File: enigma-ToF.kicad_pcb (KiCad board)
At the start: 2 copper layers, 90 x 90 mm, 16 parts, among them J1 Conn_01x05, U0 PCF8575, U1 VL53L1X, U10 VL53L1X, U15 PCF8575, U2 VL53L1X, U3 VL53L1X, U4 VL53L1X, U5 VL53L1X, U6 VL53L1X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

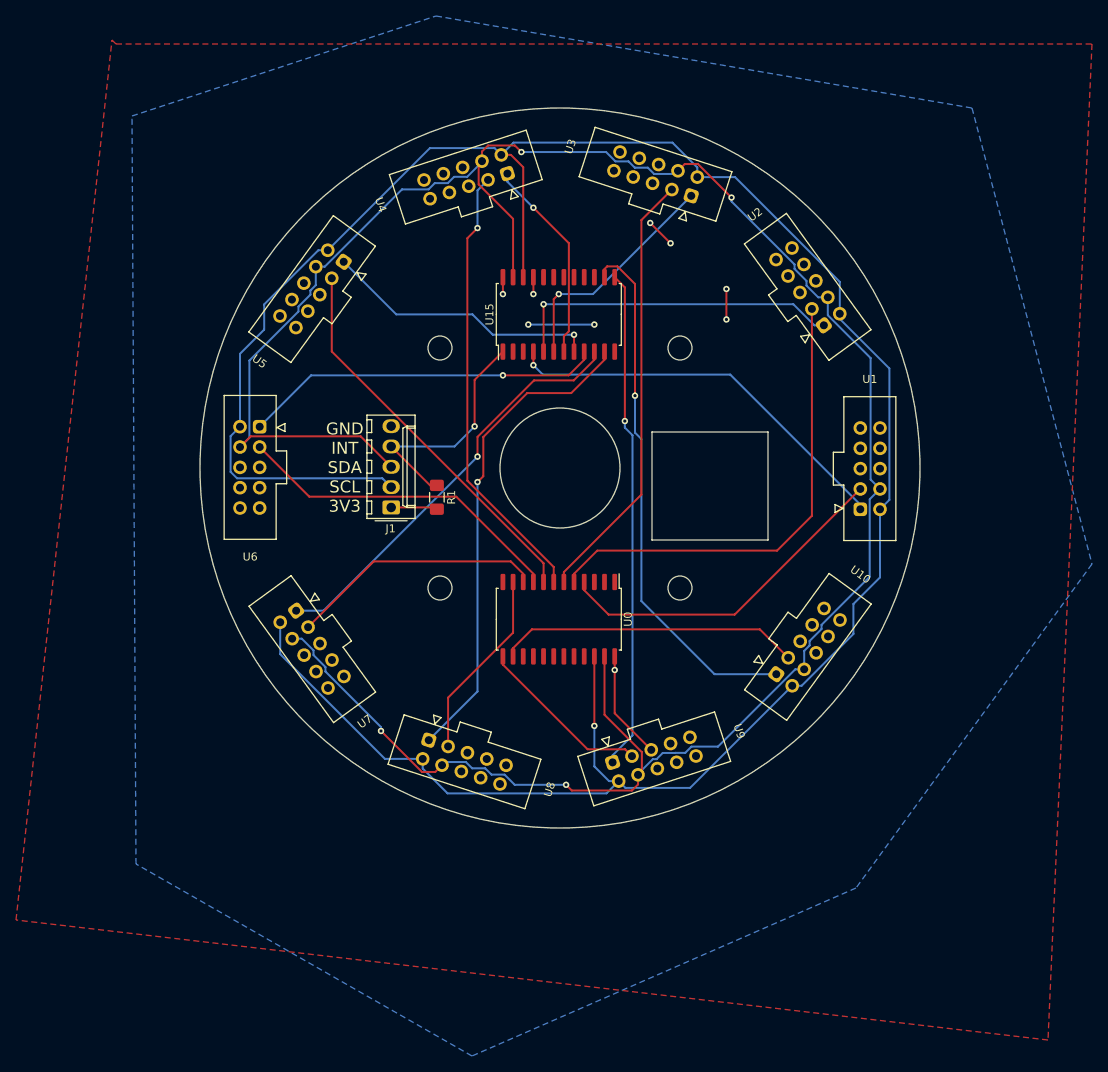
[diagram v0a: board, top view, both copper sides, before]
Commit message: Add touchpoints and power LED
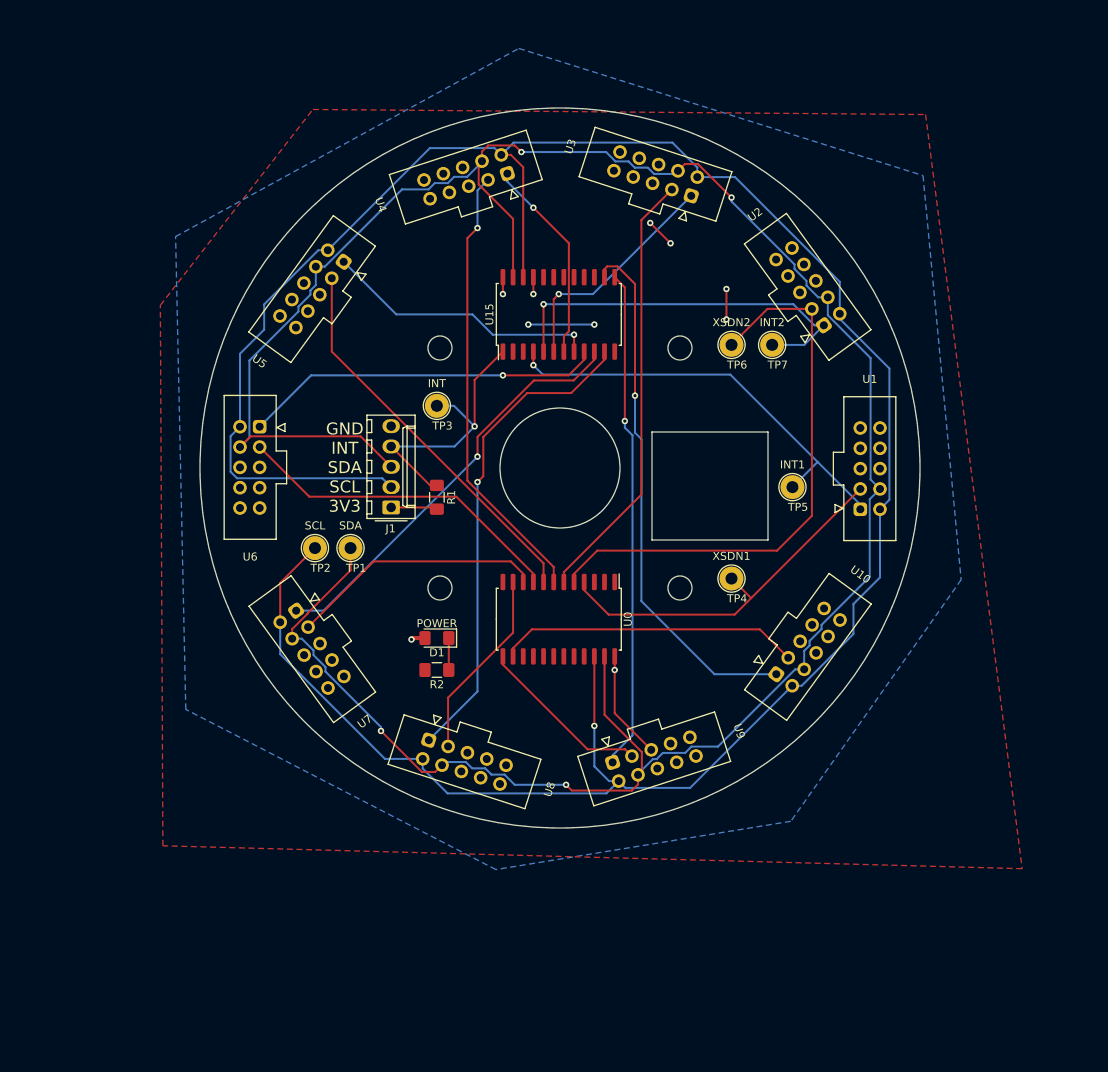
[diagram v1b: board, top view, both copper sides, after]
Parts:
- added D1: POWER, LED_SMD:LED_1206_3216Metric_Pad1.42x1.75mm_HandSolder, F.Cu at (54.6, 91.3)
- added R2: R, Resistor_SMD:R_1206_3216Metric_Pad1.42x1.75mm_HandSolder, F.Cu at (54.6, 95.2)
- added TP1: SDA, TestPoint:TestPoint_Loop_D2.54mm_Drill1.5mm_Beaded, F.Cu at (43.8, 80.0)
- added TP2: SCL, TestPoint:TestPoint_Loop_D2.54mm_Drill1.5mm_Beaded, F.Cu at (39.4, 80.0)
- added TP3: INT, TestPoint:TestPoint_Loop_D2.54mm_Drill1.5mm_Beaded, F.Cu at (54.6, 62.2)
- added TP4: XSDN1, TestPoint:TestPoint_Loop_D2.54mm_Drill1.5mm_Beaded, F.Cu at (91.4, 83.8)
- added TP5: INT1, TestPoint:TestPoint_Loop_D2.54mm_Drill1.5mm_Beaded, F.Cu at (99.1, 72.4)
- added TP6: XSDN2, TestPoint:TestPoint_Loop_D2.54mm_Drill1.5mm_Beaded, F.Cu at (91.4, 54.6)
- added TP7: INT2, TestPoint:TestPoint_Loop_D2.54mm_Drill1.5mm_Beaded, F.Cu at (96.5, 54.6)
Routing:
- net /SDA: track 295.8 -> 310.1 mm
- net /XSDN2: track 59.6 -> 71.5 mm
- net /SCL: track 308.1 -> 319.2 mm
- net /INT2: track 42.0 -> 49.5 mm
- net /INT: track 30.0 -> 35.8 mm
- net /INT1: track 50.4 -> 54.8 mm
- net Net-(D1-Pad1): track 0.00 -> 3.99 mm
- net /XSDN1: track 43.3 -> 46.8 mm
- net +3V3: track 31.0 -> 32.8 mm, vias 7 -> 8
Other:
- board text added: "The PCB is a circle of 90mm in diameter It has a 15mm diameter hole in its center and another squarish hole. It has 4 mounting points of 3mm diameter for M3 screws."

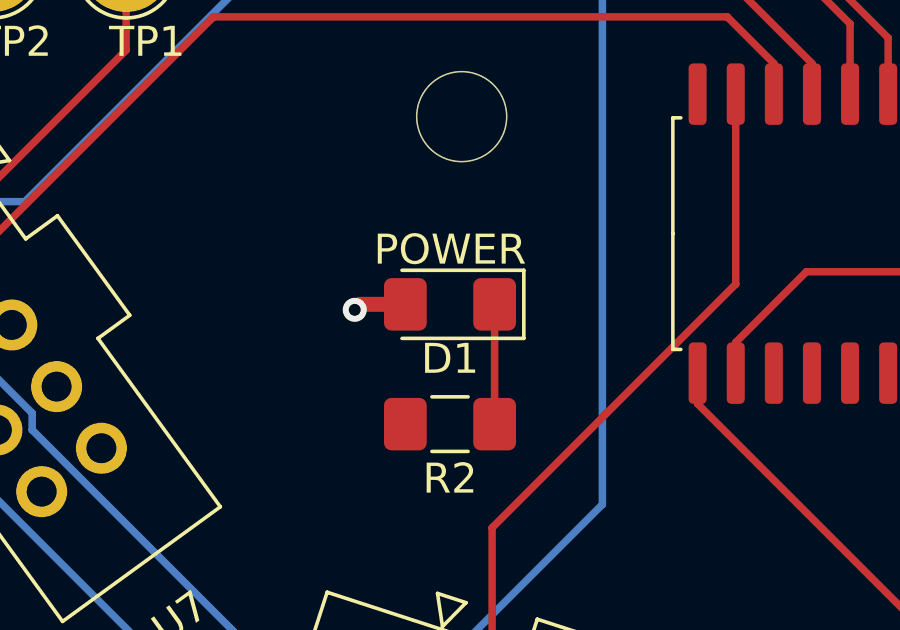
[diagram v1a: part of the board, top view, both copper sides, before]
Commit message: Change LED model and generate gerbers
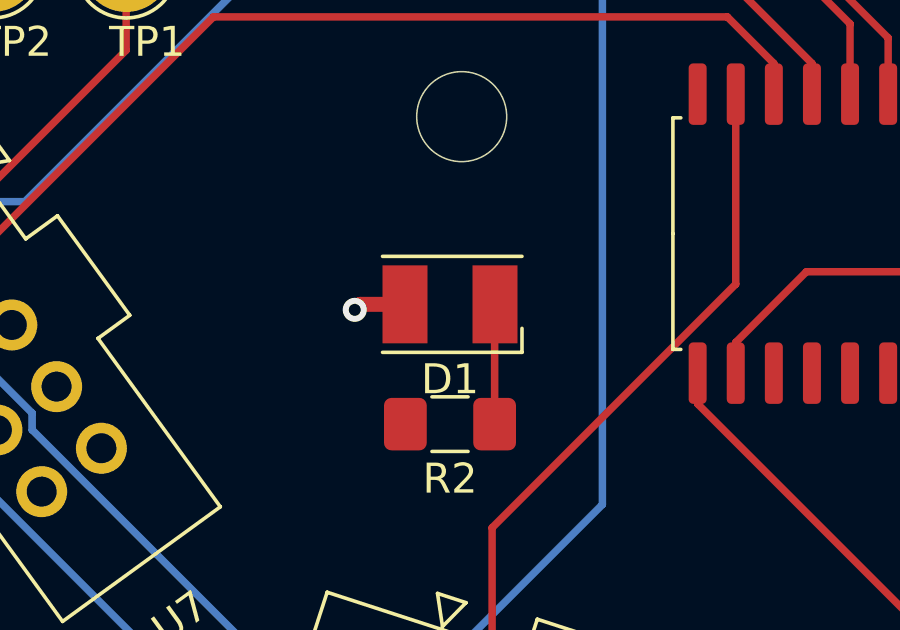
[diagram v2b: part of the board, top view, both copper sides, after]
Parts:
- D1: footprint LED_SMD:LED_1206_3216Metric_Pad1.42x1.75mm_HandSolder -> LED_SMD:LED_PLCC-2

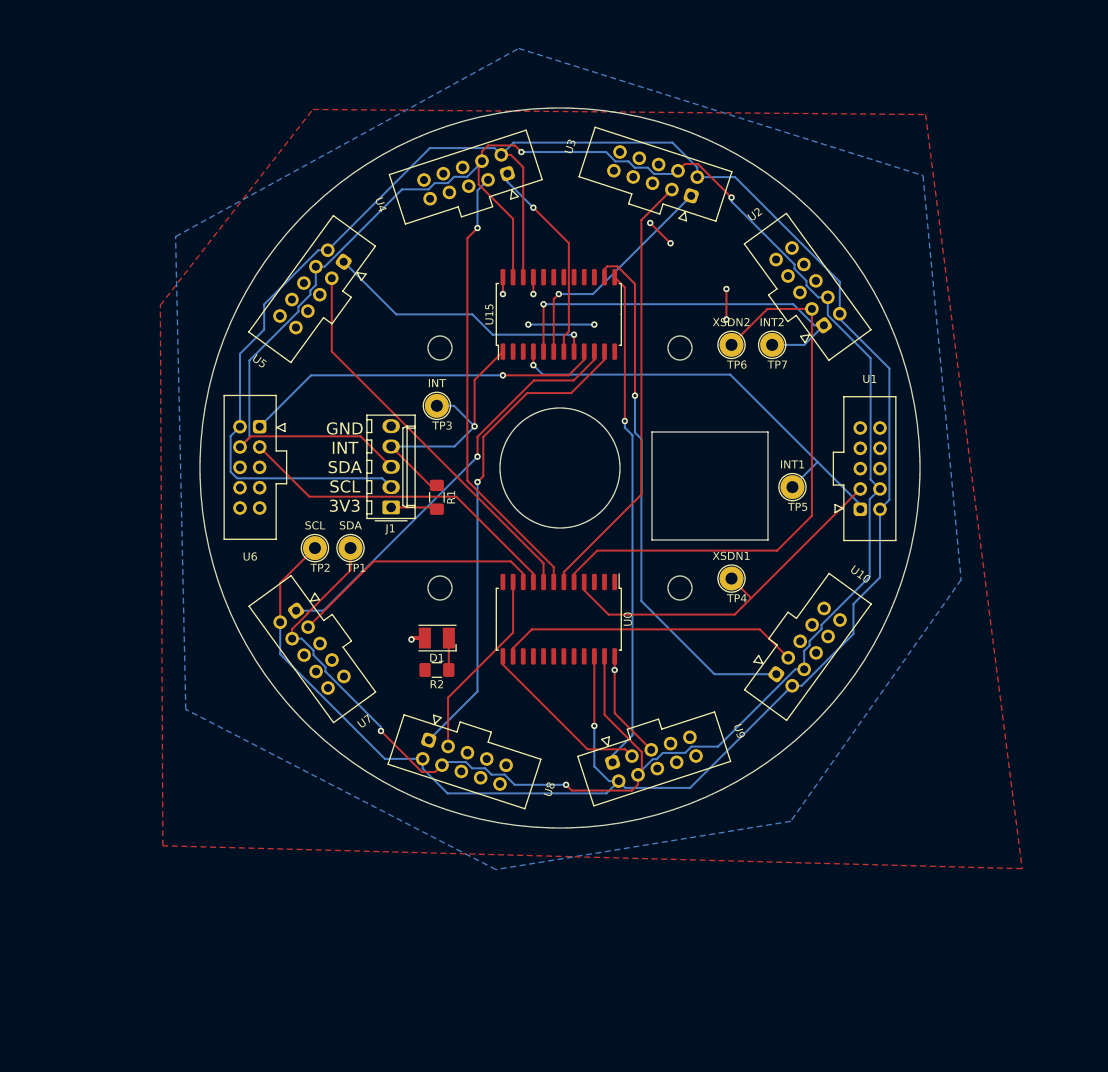
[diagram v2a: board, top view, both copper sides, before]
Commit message: Round PCB causes collisions let's do decagon
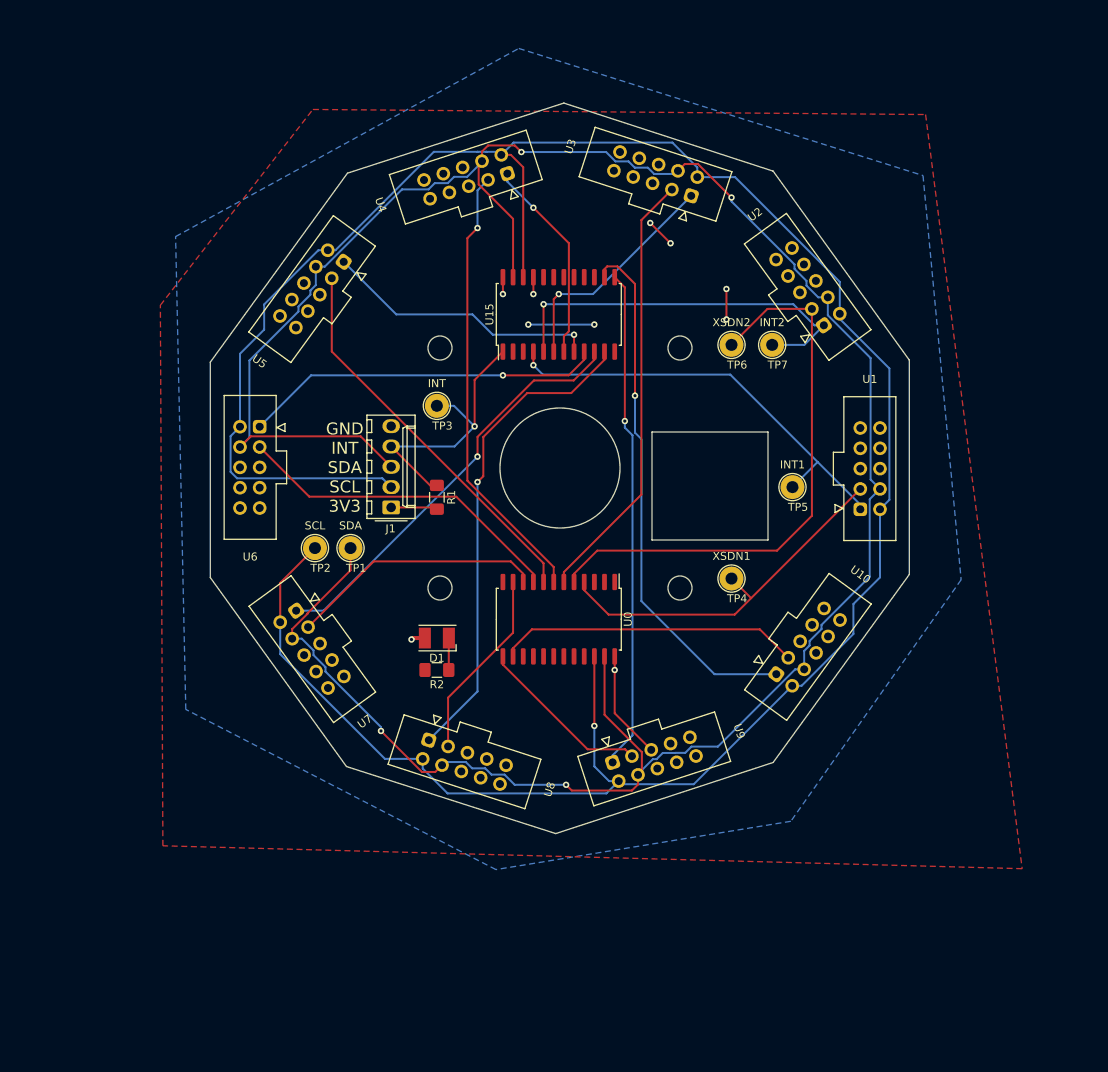
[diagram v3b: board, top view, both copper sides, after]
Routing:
- net /SCL: track 319.2 -> 318.4 mm
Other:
- board size 90 x 90 mm -> 87.4 x 91.3 mm

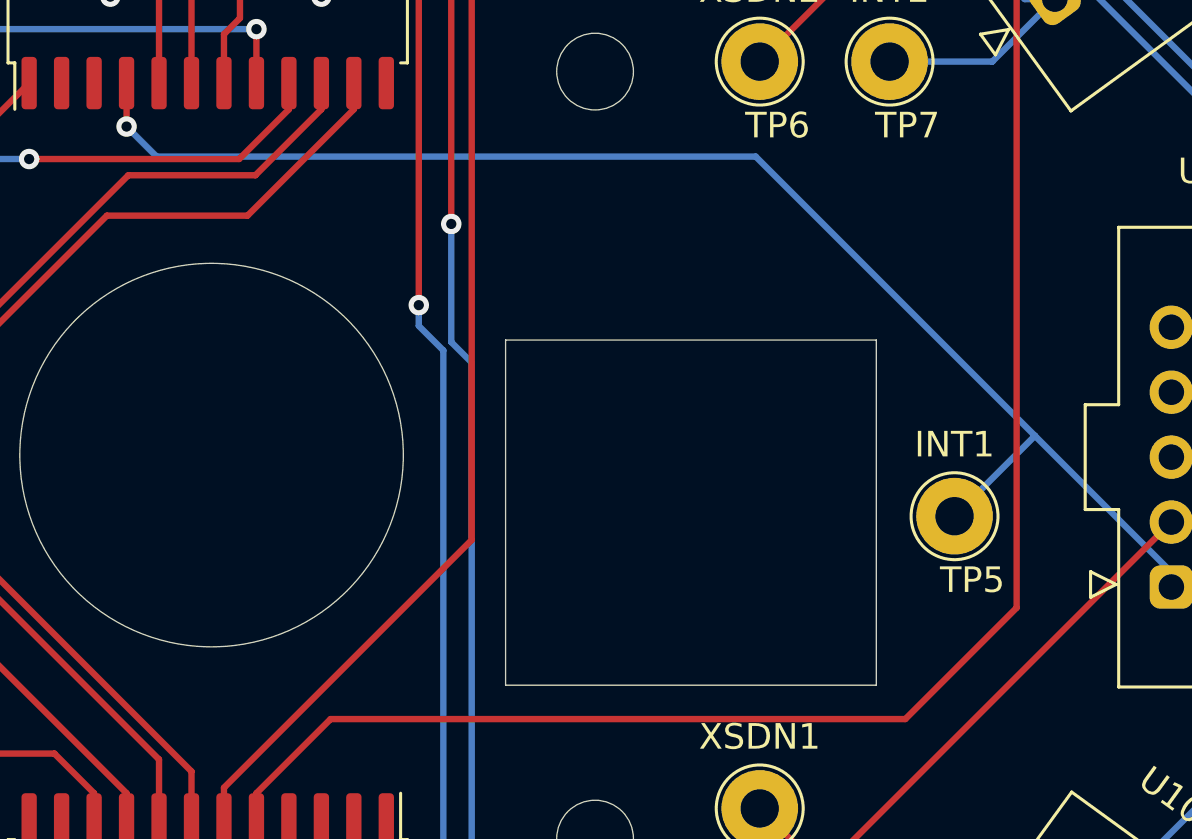
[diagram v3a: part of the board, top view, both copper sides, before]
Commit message: USB-B port on IRoise was not in the right place...
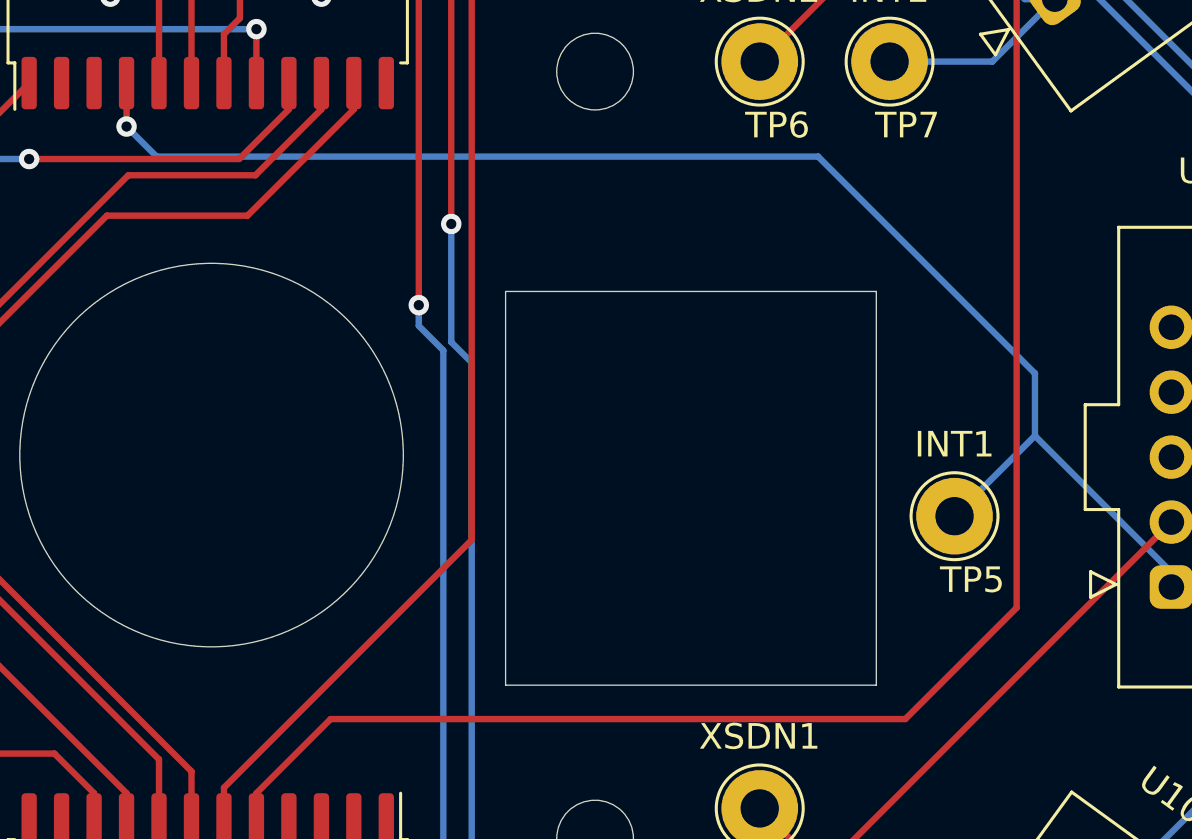
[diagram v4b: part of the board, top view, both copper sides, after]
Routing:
- net /INT1: track 54.8 -> 56.2 mm
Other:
- outline, holes or cut-outs redrawn

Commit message: Add JLCPCB silkscreen
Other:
- board text added: "JLCJLCJLCJLC"
